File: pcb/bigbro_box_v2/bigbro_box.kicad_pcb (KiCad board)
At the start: 2 copper layers, 102 x 58 mm, 51 parts, among them J1 Current Sense, J2 Display, J3 Mains, J4 UART flashing, J5 RFID, J6 Relay, K1 G5LE-1, Q1 MMBT3904, Q2 MMBT3904, Q3 BSS138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

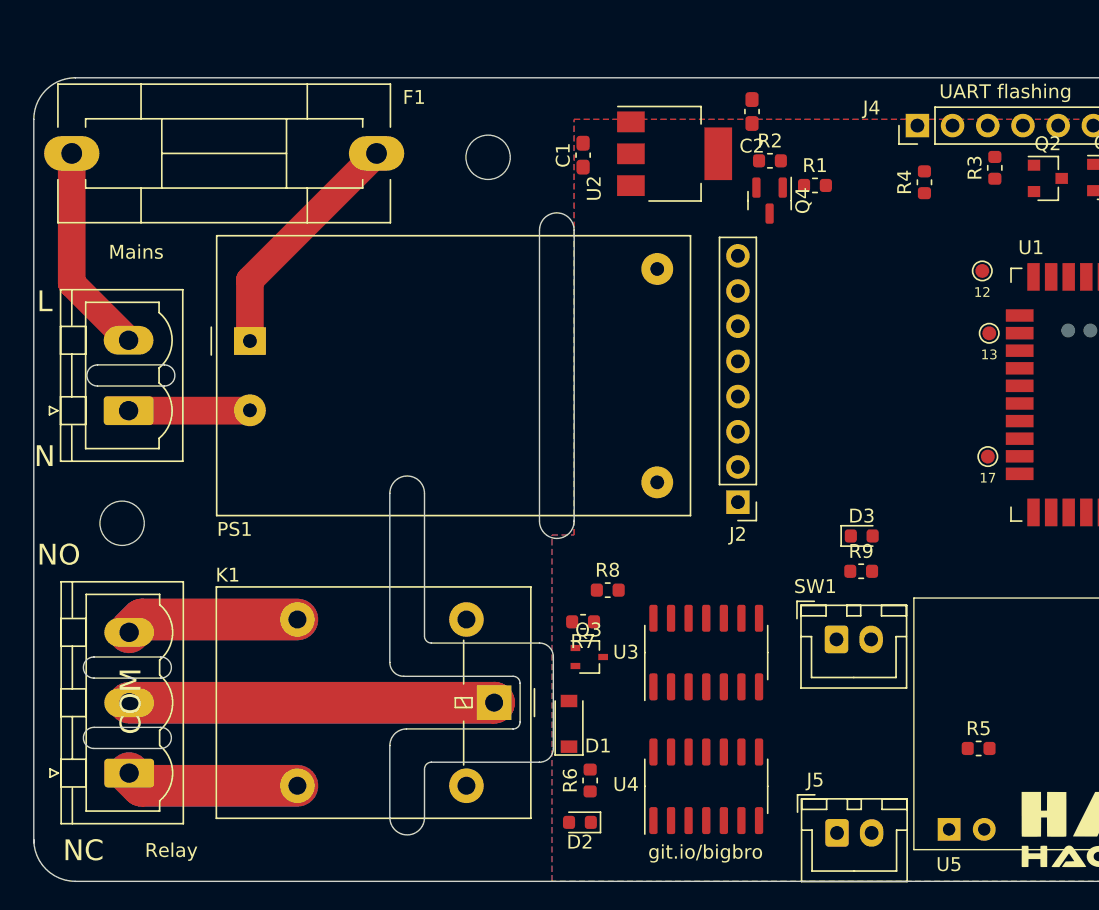
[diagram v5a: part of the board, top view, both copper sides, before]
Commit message: Add 3D model for fuse holder.
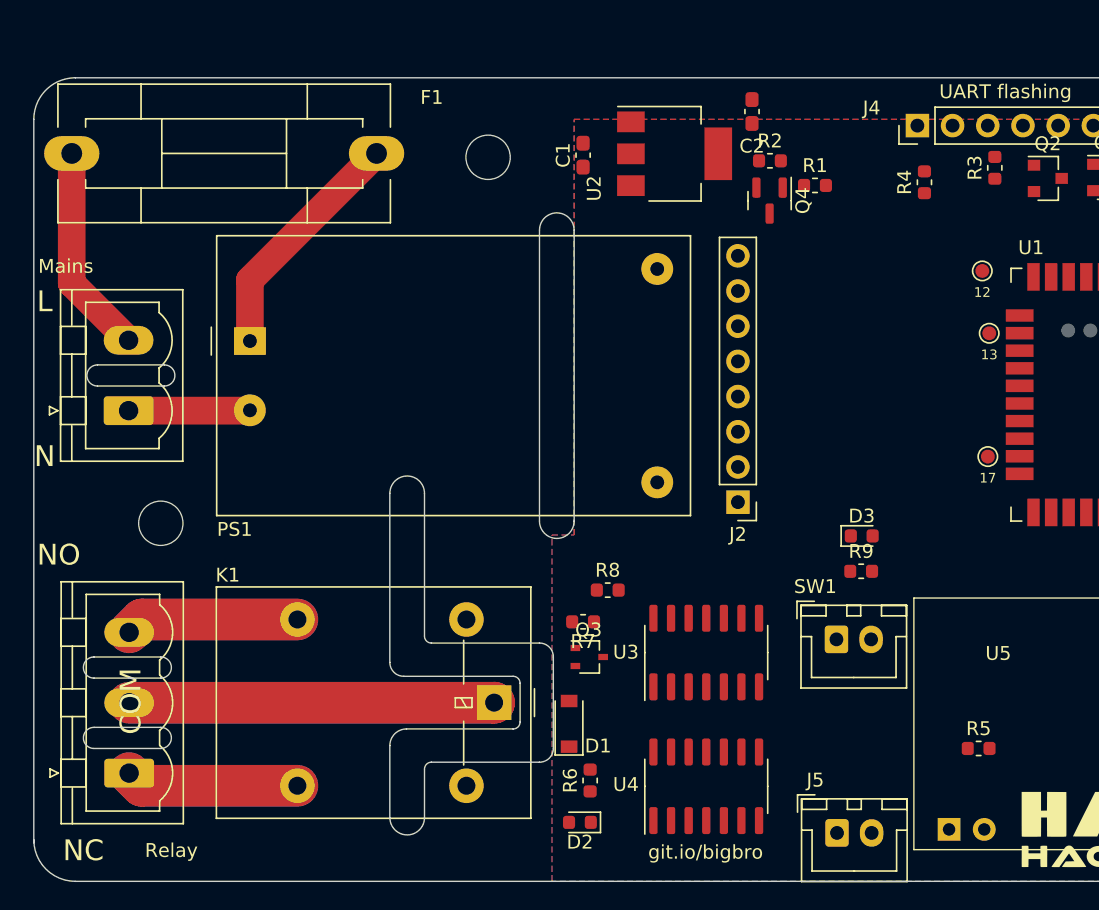
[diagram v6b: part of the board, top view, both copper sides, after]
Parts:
- moved H1 2.79 mm to (74.2, 89.2)
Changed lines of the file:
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@@
     (property "ki_keywords" "fuse")
     (attr through_hole)
-    (fp_text reference "F1" (at 24.716 -4.039) (layer "F.SilkS")
+    (fp_text reference "F1" (at 25.986 -4.039) (layer "F.SilkS")
         (effects (font (size 1 1) (thickness 0.15)))
     )
-    (fp_text value "250mA" (at 12.27 7.62) (layer "F.Fab")
+    (fp_text value "250mA" (at 25.224 0.279 90) (layer "F.Fab")
         (effects (font (size 1 1) (thickness 0.15)))
     )
@@
     (pad "2" thru_hole oval (at 22 0 270) (size 2.5 4) (drill 1.5) (layers "*.Cu" "*.Mask")
       (net 8 "Net-(PS1-AC{slash}L)") (pintype "passive"))
+    (model "${KIPRJMOD}/lib/3D/fuseholder-5x20-trans-cover.wrl"
+      (offset (xyz 12.5 0 0))
+      (scale (xyz 1 1 1))
+      (rotate (xyz 0 0 0))
+    )
   )
   (footprint "TestPoint:TestPoint_Pad_D1.0mm" (layer "F.Cu")
@@
   )
   (footprint "MountingHole:MountingHole_3.2mm_M3" (layer "F.Cu")
-    (at 71.374 89.154)
+    (at 74.168 89.154)
     (descr "Mounting Hole 3.2mm, no annular, M3")
     (tags "mounting hole 3.2mm no annular m3")
@@
         (effects (font (size 1 1) (thickness 0.15)))
     )
-    (fp_text value "MountingHole" (at 0 4.2) (layer "F.Fab")
+    (fp_text value "MountingHole" (at 0 4.2) (layer "F.Fab") hide
         (effects (font (size 1 1) (thickness 0.15)))
     )
@@
     (property "ki_keywords" "uart, rfid")
     (attr through_hole)
-    (fp_text reference "U5" (at 0 2.54) (layer "F.SilkS")
+    (fp_text reference "U5" (at 3.556 -12.7) (layer "F.SilkS")
         (effects (font (size 1 1) (thickness 0.15)))
     )
@@
         (effects (font (size 1 1) (thickness 0.15)))
     )
-    (fp_text value "Mains" (at 11.43 0.5475) (layer "F.SilkS")
+    (fp_text value "Mains" (at 10.414 -4.5325) (layer "F.SilkS")
         (effects (font (size 1 1) (thickness 0.15)))
     )
@@
         (effects (font (size 1 1) (thickness 0.15)))
     )
-    (fp_text value "MountingHole" (at 0 4.2) (layer "F.Fab")
+    (fp_text value "MountingHole" (at 0 4.2) (layer "F.Fab") hide
         (effects (font (size 1 1) (thickness 0.15)))
     )
@@
         (effects (font (size 1 1) (thickness 0.15)))
     )
-    (fp_text value "MountingHole" (at -10.637355 6.140875) (layer "F.Fab")
+    (fp_text value "MountingHole" (at -10.637355 6.140875) (layer "F.Fab") hide
         (effects (font (size 1 1) (thickness 0.15)))
     )
@@
         (effects (font (size 1 1) (thickness 0.15)))
     )
-    (fp_text value "MountingHole" (at 0 4.2) (layer "F.Fab")
+    (fp_text value "MountingHole" (at 0 4.2) (layer "F.Fab") hide
         (effects (font (size 1 1) (thickness 0.15)))
     )

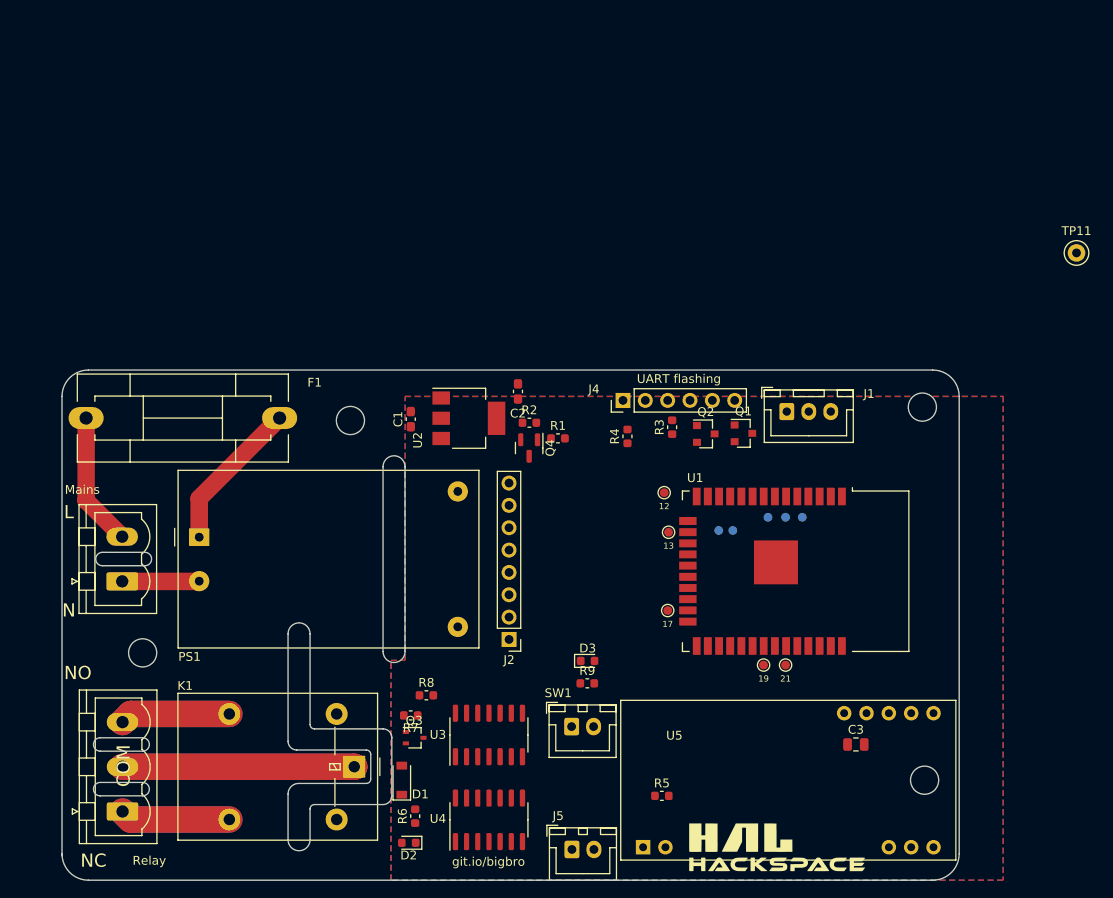
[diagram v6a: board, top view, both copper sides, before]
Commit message: Route flip-flop, reduce width to 100 mm.
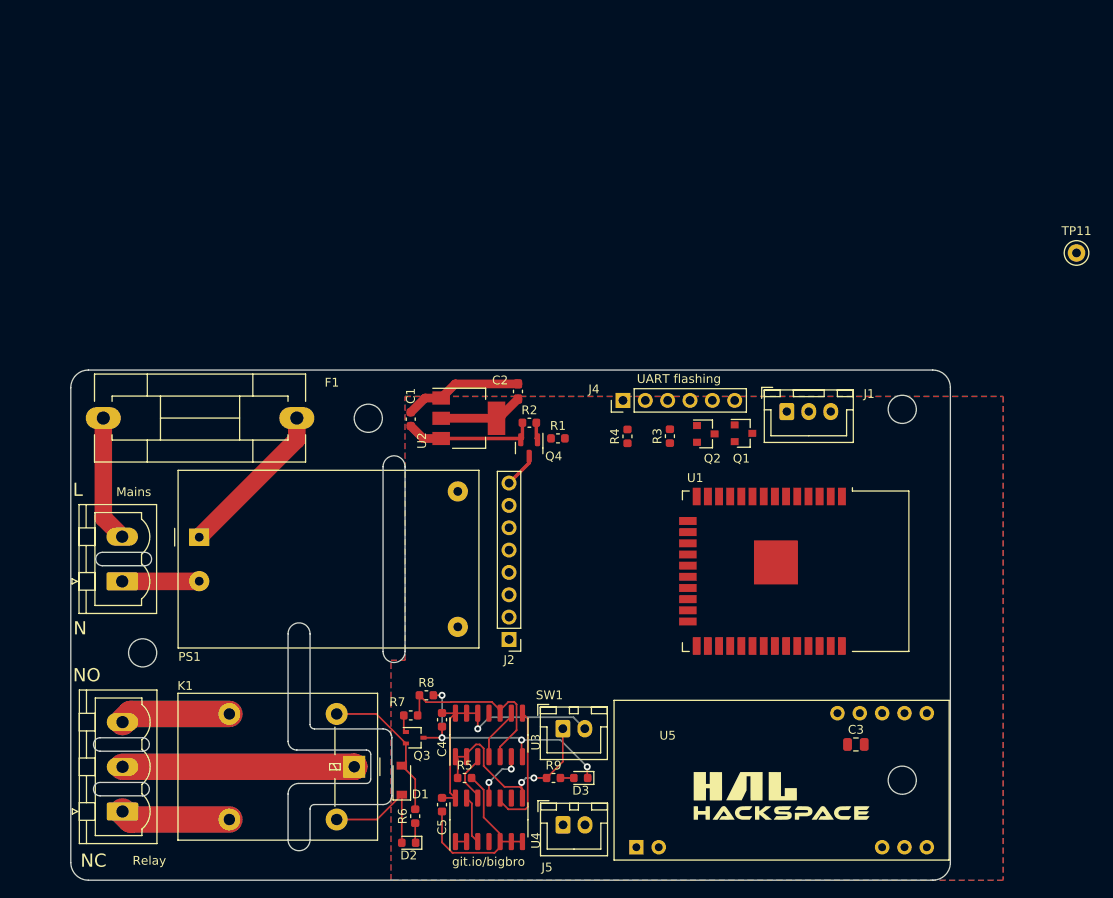
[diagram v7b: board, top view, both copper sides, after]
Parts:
- removed TP1: 12, TestPoint:TestPoint_Pad_D1.0mm
- removed TP10: 35, TestPoint:TestPoint_Pad_D1.0mm
- removed TP2: 13, TestPoint:TestPoint_Pad_D1.0mm
- removed TP3: 14, TestPoint:TestPoint_Pad_D1.0mm
- removed TP4: 17, TestPoint:TestPoint_Pad_D1.0mm
- removed TP5: 19, TestPoint:TestPoint_Pad_D1.0mm
- removed TP6: 21, TestPoint:TestPoint_Pad_D1.0mm
- removed TP7: 27, TestPoint:TestPoint_Pad_D1.0mm
- removed TP8: 32, TestPoint:TestPoint_Pad_D1.0mm
- removed TP9: 34, TestPoint:TestPoint_Pad_D1.0mm
- added C4: 100n, Capacitor_SMD:C_0603_1608Metric, F.Cu at (108.2, 96.8)
- added C5: 100n, Capacitor_SMD:C_0603_1608Metric, F.Cu at (108.2, 106.4)
- C1: footprint Capacitor_SMD:C_0603_1608Metric_Pad1.08x0.95mm_HandSolder -> Capacitor_SMD:C_0603_1608Metric
- moved R5 22.5 mm to (110.8, 103.4)
- moved D3 13.3 mm to (124.0, 103.4), turned to 180 degrees
- moved R9 11.4 mm to (120.9, 103.4)
- moved G*** 5.86 mm to (146.8, 105.4)
- moved J5 2.97 mm to (122.0, 108.7)
- moved H4 2.54 mm to (160.5, 103.6)
- moved H3 2.30 mm to (160.5, 61.5)
- moved H2 2.05 mm to (99.8, 62.5)
- moved F1 1.95 mm to (69.7, 62.5)
- moved R3 1.05 mm to (134.1, 64.5)
- moved SW1 1.02 mm to (121.9, 97.8)
- moved U5 0.76 mm to (130.3, 111.3)
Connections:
- U1 pad 12: Net-(U1-IO27) -> unconnected-(U1-IO27-Pad12)
- U1 pad 13: Net-(U1-IO14) -> unconnected-(U1-IO14-Pad13)
- U1 pad 14: Net-(U1-IO12) -> unconnected-(U1-IO12-Pad14)
- U1 pad 16: Net-(U1-IO13) -> unconnected-(U1-IO13-Pad16)
- U1 pad 28: Net-(U1-IO17) -> unconnected-(U1-IO17-Pad28)
- U1 pad 31: Net-(U1-IO19) -> unconnected-(U1-IO19-Pad31)
- U1 pad 33: Net-(U1-IO21) -> unconnected-(U1-IO21-Pad33)
- U1 pad 6: Net-(U1-IO34) -> unconnected-(U1-IO34-Pad6)
- U1 pad 7: Net-(U1-IO35) -> unconnected-(U1-IO35-Pad7)
- U1 pad 8: Net-(U1-IO32) -> unconnected-(U1-IO32-Pad8)
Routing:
- net GND: track 0.00 -> 66.5 mm, vias 0 -> 4
- net +3V3: track 0.00 -> 40.4 mm, vias 0 -> 1
- net +5V: track 0.00 -> 29.2 mm
- net /card_switch: track 0.00 -> 26.5 mm, vias 0 -> 2
- net /relay: track 0.00 -> 21.7 mm
- net Net-(D1-A): track 0.00 -> 17.6 mm
- net /Relay_trig: track 0.00 -> 14.9 mm
- net /Relay_reset: track 0.00 -> 6.35 mm, vias 0 -> 2
- net Net-(U3-Pad4): track 0.00 -> 6.00 mm
- net /~{relay_gpio}: track 0.00 -> 5.90 mm
- net /~{card_switch}: track 0.00 -> 5.48 mm
- net Display_Led: track 0.00 -> 3.99 mm
- net Net-(D2-K): track 0.00 -> 2.26 mm
- net Net-(Q4-B): track 0.00 -> 1.99 mm
- net Net-(Q3-G): track 0.00 -> 1.99 mm
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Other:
- board size 102 x 58 mm -> 100 x 58 mm
- board text removed: "COM"

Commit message: Finish routing.
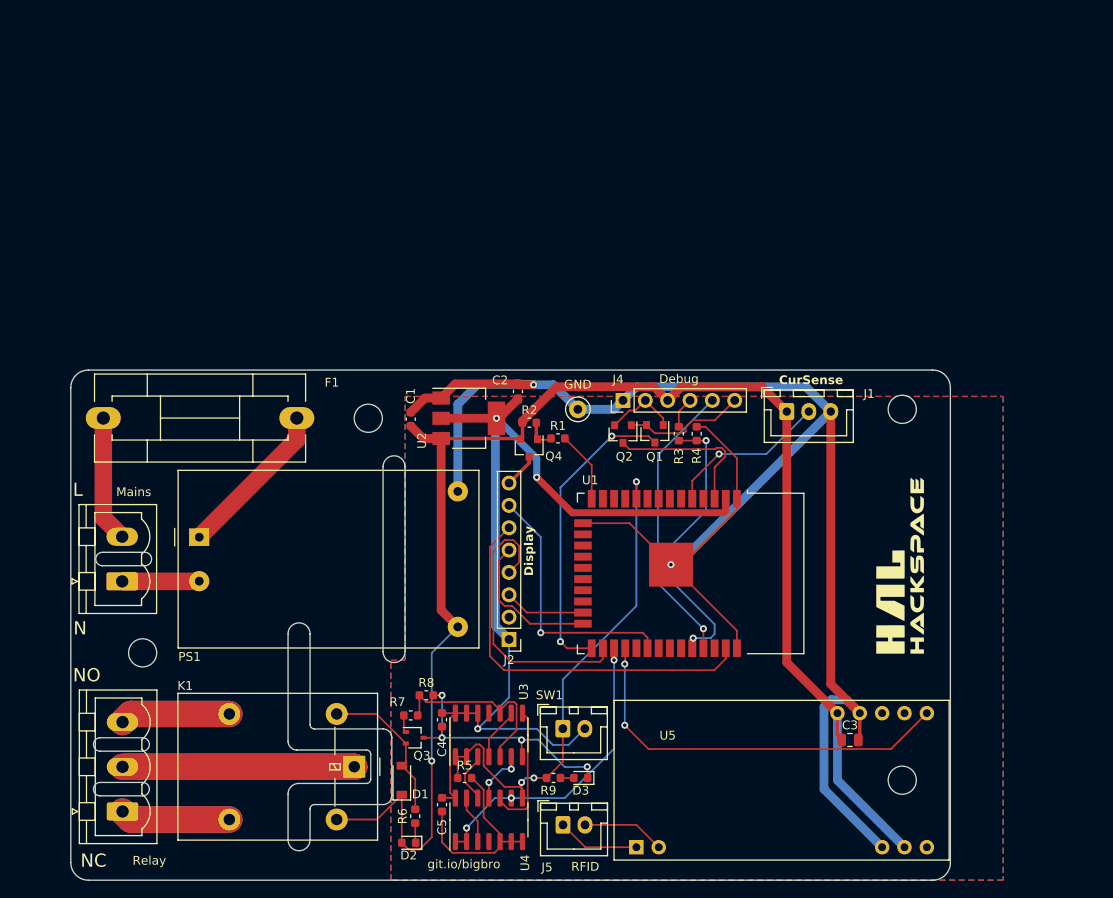
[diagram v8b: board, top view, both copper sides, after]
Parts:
- J4: value UART flashing -> Debug
- moved TP11 59.4 mm to (123.6, 61.5)
- moved G*** 29.4 mm to (160.3, 79.2), turned to 90 degrees
- moved U1 11.9 mm to (133.5, 80.1)
- moved Q1 10.1 mm to (132.4, 64.2), turned to -90 degrees
- moved Q2 9.41 mm to (128.8, 64.3), turned to -90 degrees
- moved R4 7.88 mm to (137.2, 64.2)
- moved G*** 2.81 mm to (145.7, 111.7)
- moved R3 1.05 mm to (135.1, 64.2), turned to -90 degrees
- moved C3 0.85 mm to (154.6, 99.1)
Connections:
- U1 pad 14: unconnected-(U1-IO12-Pad14) -> Display_backlight
- U1 pad 27: ESP_RFID_TX -> /relay_gpio
- U1 pad 28: unconnected-(U1-IO17-Pad28) -> ESP_RFID_TX
- U1 pad 29: Display_backlight -> unconnected-(U1-IO5-Pad29)
- U1 pad 9: /relay_gpio -> unconnected-(U1-IO33-Pad9)
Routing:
- net GND: track 66.5 -> 259.5 mm, vias 4 -> 6
- net +5V: track 29.2 -> 173.5 mm, vias 0 -> 1
- net +3V3: track 40.4 -> 111.6 mm, vias 1 -> 3
- net ESP_RFID_TX: track 0.00 -> 45.9 mm, vias 0 -> 2
- net Display_SDA: track 0.00 -> 44.7 mm
- net /~{BOOT}: track 0.00 -> 34.8 mm, vias 0 -> 2
- net /relay_gpio: track 1.27 -> 34.8 mm, vias 0 -> 3
- net /MCU_RX0: track 0.00 -> 33.5 mm, vias 0 -> 2
- net /card_switch: track 26.5 -> 59.9 mm, vias 2 -> 3
- net /MCU_TX0: track 0.00 -> 32.9 mm, vias 0 -> 1
- net Display_Reset: track 0.00 -> 32.4 mm
- net Display_SCk: track 0.00 -> 29.5 mm, vias 0 -> 1
- net /CurrentSense: track 0.00 -> 18.5 mm, vias 0 -> 1
- net /~{RESET}: track 0.00 -> 18.0 mm
- net Display_A0: track 0.00 -> 16.8 mm
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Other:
- board text added: "CurSense"
- board text added: "Display"
- board text added: "GND"
- board text added: "RFID"
